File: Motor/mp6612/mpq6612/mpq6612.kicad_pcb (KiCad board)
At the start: 2 copper layers, 33 x 34 mm, 31 parts, among them J1 Conn_01x07, J2 OQ0212500000G, U1 MP6612DGF-P

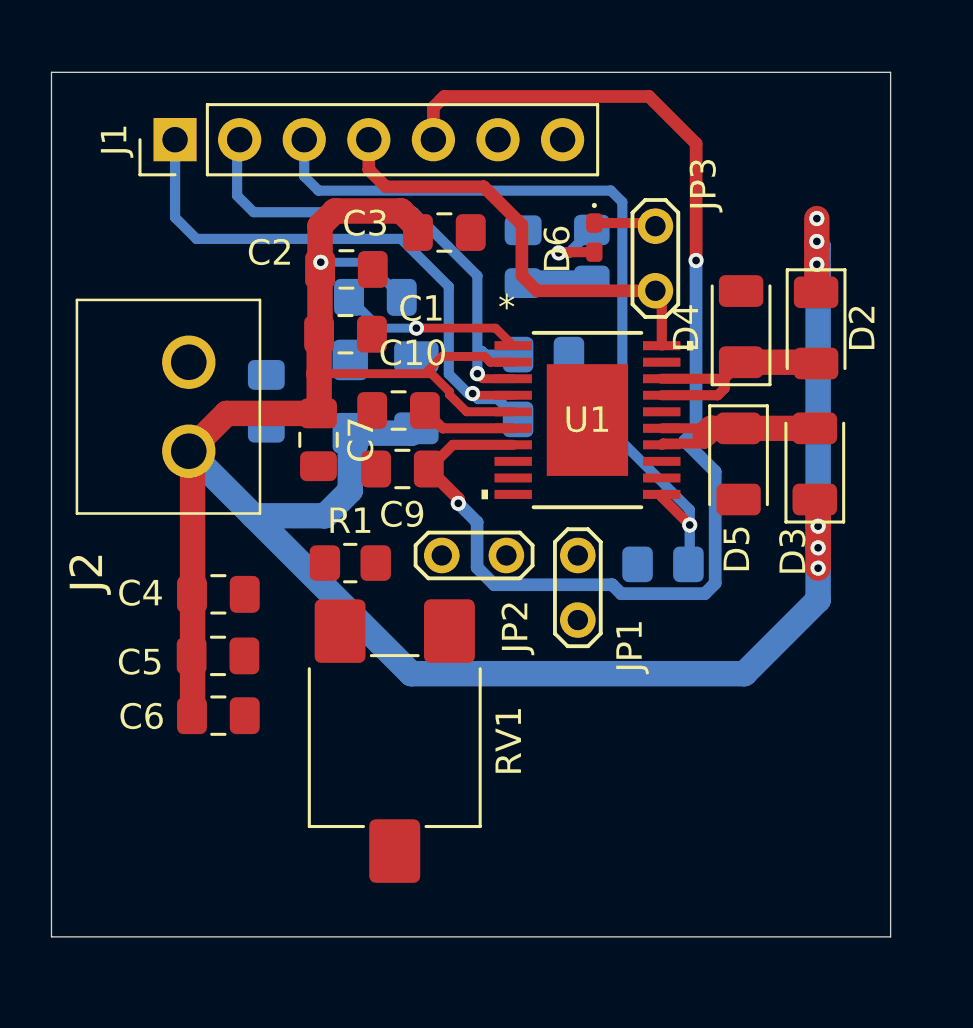
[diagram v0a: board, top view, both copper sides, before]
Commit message: Layout
Update layouts for the motor drivers
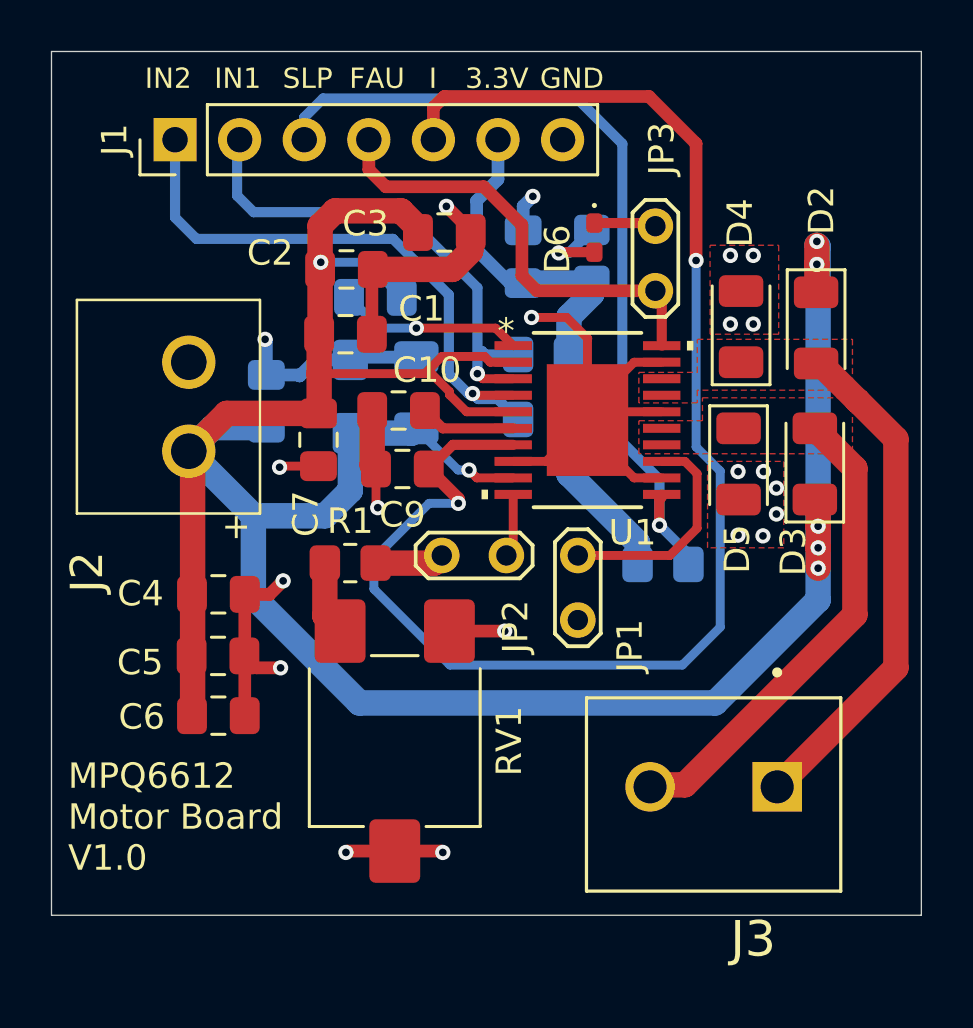
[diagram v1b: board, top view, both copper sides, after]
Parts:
- added J3: TB002-500-02BE, User_Footprint:CUI_TB002-500-02BE, F.Cu at (167.5, 101.1)
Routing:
- net GND: track 0.00 -> 58.3 mm, vias 0 -> 21
- net +3.3V: track 2.74 -> 22.3 mm
- net /Out1: track 9.32 -> 19.9 mm
- net /Out2: track 8.44 -> 18.7 mm
- net /visen: track 48.9 -> 58.4 mm
- net /Vin: track 102.7 -> 111.7 mm
- net Net-(JP1-A): track 0.00 -> 8.87 mm
- net Net-(R1-Pad1): track 0.00 -> 2.92 mm
- net Net-(JP2-A): track 0.00 -> 2.72 mm
- net Net-(JP2-B): track 0.00 -> 2.51 mm
- net /~{sleep}: track 31.4 -> 33.3 mm
- added copper zone on F.Cu, net /Out1
- added copper zone on F.Cu, net /Out2
- added copper zone on F.Cu, net GND
- added copper zone on In1.Cu, net GND
- added copper zone on In2.Cu, net GND
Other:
- board size 33 x 34 mm -> 34.2 x 34 mm
- copper layers 2 -> 4
- board text added: "+"
- board text added: "3.3V"
- board text added: "FAU"
- board text added: "GND"
- board text added: "I"
- board text added: "IN1"
- board text added: "IN2"
- board text added: "JP1 OVER CURRENT ADJ JP2 CURRENT SET JP3 LED FAULT"
- board text added: "MPQ6612 Motor Board V1.0"
- board text added: "SLP"
